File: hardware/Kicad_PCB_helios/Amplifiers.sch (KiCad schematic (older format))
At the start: 38 parts, among them U6 TL084_v, U7 LM358, U8 TL084_v

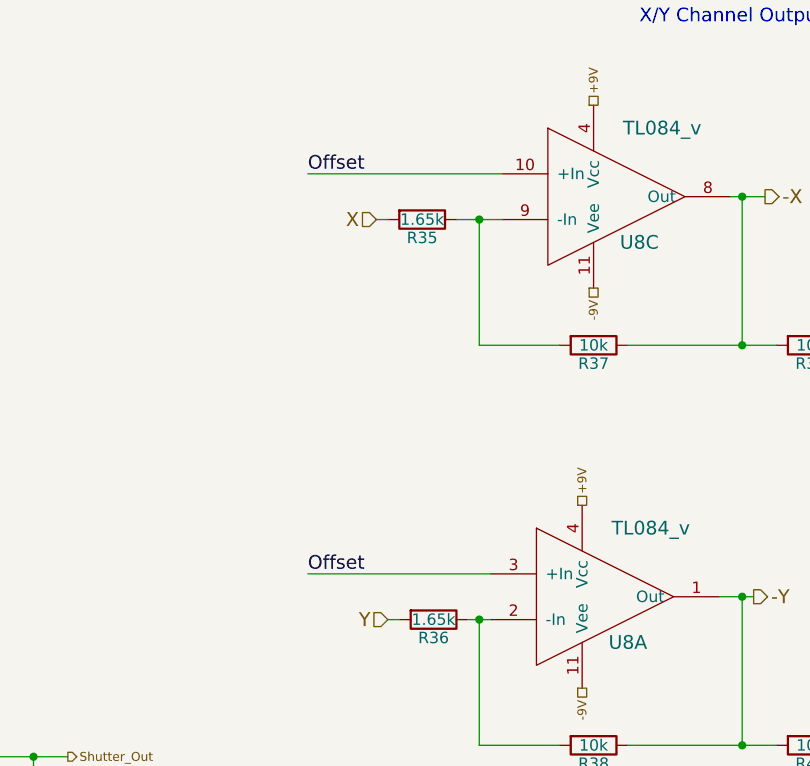
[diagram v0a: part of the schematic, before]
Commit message: fix some outdated schematics
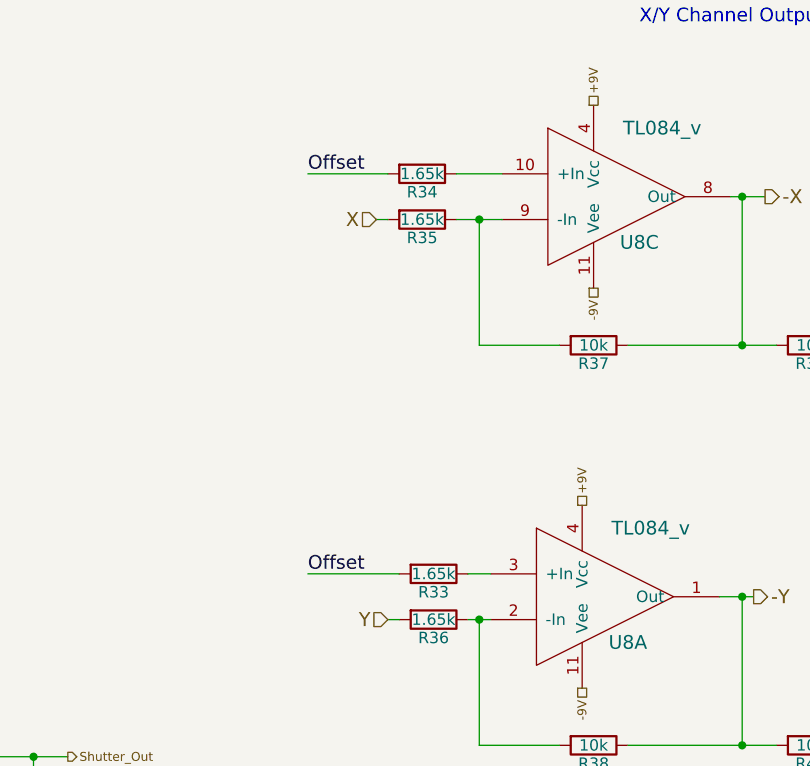
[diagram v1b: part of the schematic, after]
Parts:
- added R33, R34: 1.65k, Resistors_SMD:R_0603, symbol R
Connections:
- net Offset: now also R33.2, R34.2; no longer U8.10 (+In), U8.3 (+In)
- new net: R33.1, U8.3 (+In)
- new net: R34.1, U8.10 (+In)
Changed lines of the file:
@@
 EESchema Schematic File Version 2
+LIBS:Helios-rescue
 LIBS:power
 LIBS:device
@@
 2.5V
 $Comp
-L GND #PWR16
+L GND #PWR018
 U 1 1 56D62C05
 P 900 6950
-F 0 "#PWR16" H 900 6700 50  0001 C CNN
+F 0 "#PWR018" H 900 6700 50  0001 C CNN
 F 1 "GND" H 900 6800 50  0000 C CNN
 F 2 "" H 900 6950 50  0000 C CNN
@@
 $EndComp
 $Comp
-L GND #PWR22
+L GND #PWR019
 U 1 1 56D64930
 P 4600 7450
-F 0 "#PWR22" H 4600 7200 50  0001 C CNN
+F 0 "#PWR019" H 4600 7200 50  0001 C CNN
 F 1 "GND" H 4600 7300 50  0000 C CNN
 F 2 "" H 4600 7450 50  0000 C CNN
@@
 $EndComp
 $Comp
-L GND #PWR19
+L GND #PWR020
 U 1 1 56E9F32E
 P 2800 7400
-F 0 "#PWR19" H 2800 7150 50  0001 C CNN
+F 0 "#PWR020" H 2800 7150 50  0001 C CNN
 F 1 "GND" H 2800 7250 50  0000 C CNN
 F 2 "" H 2800 7400 50  0000 C CNN
@@
 +9V
 $Comp
-L GND #PWR26
+L GND #PWR021
 U 1 1 56EA45CC
 P 9450 5000
-F 0 "#PWR26" H 9450 4750 50  0001 C CNN
+F 0 "#PWR021" H 9450 4750 50  0001 C CNN
 F 1 "GND" H 9450 4850 50  0000 C CNN
 F 2 "" H 9450 5000 50  0000 C CNN
@@
 -9V
 $Comp
-L GND #PWR17
+L GND #PWR022
 U 1 1 56EA914F
 P 1350 2350
-F 0 "#PWR17" H 1350 2100 50  0001 C CNN
+F 0 "#PWR022" H 1350 2100 50  0001 C CNN
 F 1 "GND" H 1350 2200 50  0000 C CNN
 F 2 "" H 1350 2350 50  0000 C CNN
@@
 -9V
 $Comp
-L GND #PWR18
+L GND #PWR023
 U 1 1 56EAC37C
 P 1350 4200
-F 0 "#PWR18" H 1350 3950 50  0001 C CNN
+F 0 "#PWR023" H 1350 3950 50  0001 C CNN
 F 1 "GND" H 1350 4050 50  0000 C CNN
 F 2 "" H 1350 4200 50  0000 C CNN
@@
 -9V
 $Comp
-L GND #PWR20
+L GND #PWR024
 U 1 1 56EADE6C
 P 3650 4150
-F 0 "#PWR20" H 3650 3900 50  0001 C CNN
+F 0 "#PWR024" H 3650 3900 50  0001 C CNN
 F 1 "GND" H 3650 4000 50  0000 C CNN
 F 2 "" H 3650 4150 50  0000 C CNN
@@
 +9V
 $Comp
-L GND #PWR23
+L GND #PWR025
 U 1 1 56ECCA82
 P 9450 1400
-F 0 "#PWR23" H 9450 1150 50  0001 C CNN
+F 0 "#PWR025" H 9450 1150 50  0001 C CNN
 F 1 "GND" H 9450 1250 50  0000 C CNN
 F 2 "" H 9450 1400 50  0000 C CNN
@@
 $EndComp
 $Comp
-L GND #PWR27
+L GND #PWR026
 U 1 1 56ECCB03
 P 9900 1400
-F 0 "#PWR27" H 9900 1150 50  0001 C CNN
+F 0 "#PWR026" H 9900 1150 50  0001 C CNN
 F 1 "GND" H 9900 1250 50  0000 C CNN
 F 2 "" H 9900 1400 50  0000 C CNN
@@
 $EndComp
 $Comp
-L GND #PWR29
+L GND #PWR027
 U 1 1 56ECCB7D
 P 10450 1400
-F 0 "#PWR29" H 10450 1150 50  0001 C CNN
+F 0 "#PWR027" H 10450 1150 50  0001 C CNN
 F 1 "GND" H 10450 1250 50  0000 C CNN
 F 2 "" H 10450 1400 50  0000 C CNN
@@
 $EndComp
 $Comp
-L GND #PWR24
+L GND #PWR028
 U 1 1 56ECD060
 P 9450 2200
-F 0 "#PWR24" H 9450 1950 50  0001 C CNN
+F 0 "#PWR028" H 9450 1950 50  0001 C CNN
 F 1 "GND" H 9450 2050 50  0000 C CNN
 F 2 "" H 9450 2200 50  0000 C CNN
@@
 $EndComp
 $Comp
-L GND #PWR28
+L GND #PWR029
 U 1 1 56ECD066
 P 9900 2200
-F 0 "#PWR28" H 9900 1950 50  0001 C CNN
+F 0 "#PWR029" H 9900 1950 50  0001 C CNN
 F 1 "GND" H 9900 2050 50  0000 C CNN
 F 2 "" H 9900 2200 50  0000 C CNN
@@
 $EndComp
 $Comp
-L GND #PWR30
+L GND #PWR030
 U 1 1 56ECD06C
 P 10450 2200
-F 0 "#PWR30" H 10450 1950 50  0001 C CNN
+F 0 "#PWR030" H 10450 1950 50  0001 C CNN
 F 1 "GND" H 10450 2050 50  0000 C CNN
 F 2 "" H 10450 2200 50  0000 C CNN
@@
 	2800 6400 2800 6550
 Wire Wire Line
-	7050 3600 7900 3600
-Wire Wire Line
-	7050 5350 7850 5350
-Wire Wire Line
 	7350 3800 7400 3800
 Wire Wire Line
@@
 $EndComp
 $Comp
-L GND #PWR25
+L GND #PWR031
 U 1 1 5792E9B8
 P 9450 3250
-F 0 "#PWR25" H 9450 3000 50  0001 C CNN
+F 0 "#PWR031" H 9450 3000 50  0001 C CNN
 F 1 "GND" H 9450 3100 50  0000 C CNN
 F 2 "" H 9450 3250 50  0000 C CNN
@@
 +9V
 $Comp
-L GND #PWR21
+L GND #PWR032
 U 1 1 56EAAE4F
 P 3700 2350
-F 0 "#PWR21" H 3700 2100 50  0001 C CNN
+F 0 "#PWR032" H 3700 2100 50  0001 C CNN
 F 1 "GND" H 3700 2200 50  0000 C CNN
 F 2 "" H 3700 2350 50  0000 C CNN
@@
 	1650 3850 1350 3850
 Connection ~ 1350 3850
+$Comp
+L R R34
+U 1 1 5CE1E9E1
+P 7550 3600
+F 0 "R34" V 7630 3600 50  0000 C CNN
+F 1 "1.65k" V 7550 3600 50  0000 C CNN
+F 2 "Resistors_SMD:R_0603" V 7480 3600 50  0001 C CNN
+F 3 "" H 7550 3600 50  0000 C CNN
+	1    7550 3600
+	0    1    1    0
+$EndComp
+Wire Wire Line
+	7400 3600 7050 3600
+Wire Wire Line
+	7700 3600 7900 3600
+$Comp
+L R R33
+U 1 1 5CE1F102
+P 7600 5350
+F 0 "R33" V 7680 5350 50  0000 C CNN
+F 1 "1.65k" V 7600 5350 50  0000 C CNN
+F 2 "Resistors_SMD:R_0603" V 7530 5350 50  0001 C CNN
+F 3 "" H 7600 5350 50  0000 C CNN
+	1    7600 5350
+	0    1    1    0
+$EndComp
+Wire Wire Line
+	7850 5350 7750 5350
+Wire Wire Line
+	7450 5350 7050 5350
 $EndSCHEMATC
